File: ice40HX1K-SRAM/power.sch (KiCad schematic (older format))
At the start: 7 parts

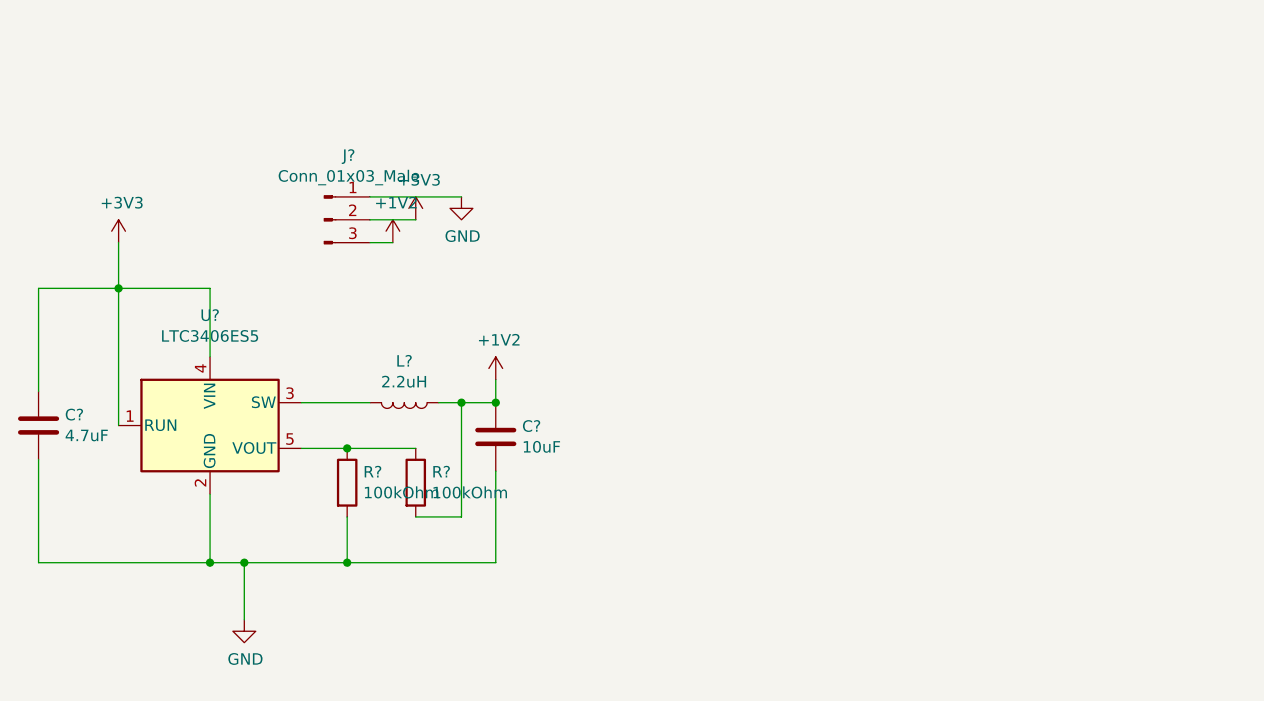
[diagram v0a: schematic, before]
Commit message: Started USB => ice40 HX1K Bridge with ATSAMD11C14A
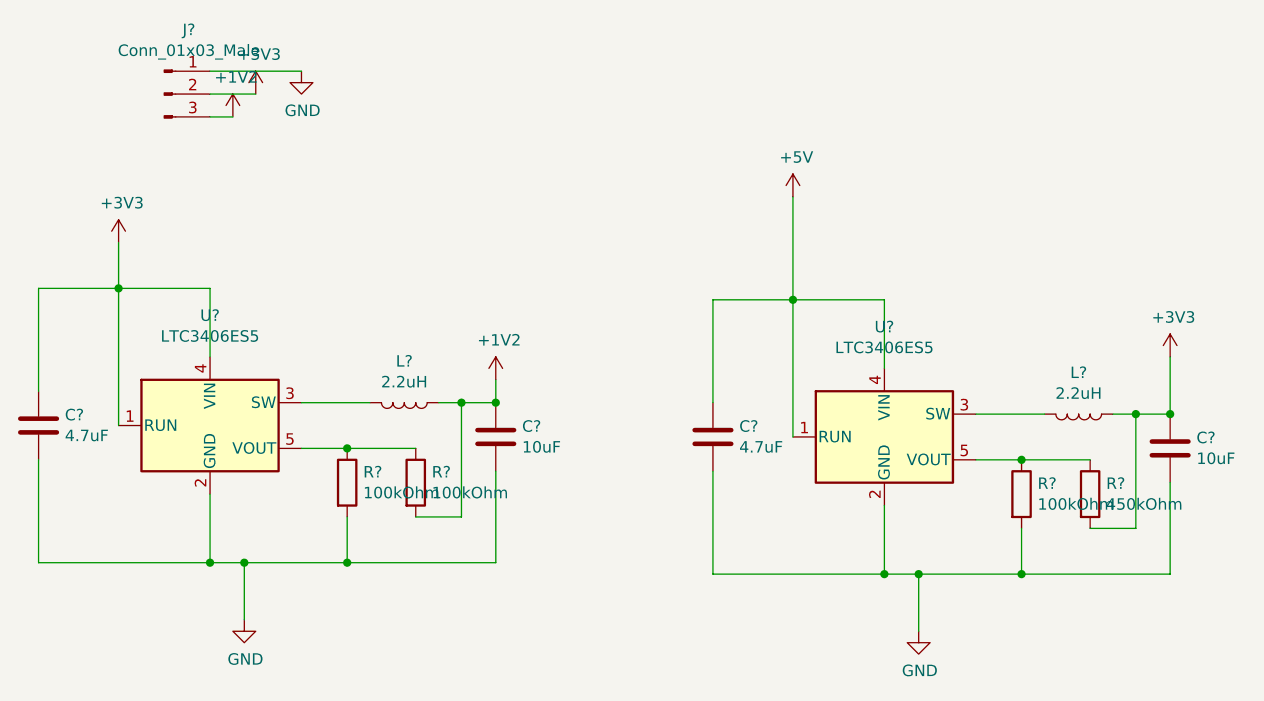
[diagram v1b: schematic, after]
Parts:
- added C?: 10uF, Capacitor_SMD:C_1206_3216Metric, symbol Device:C
- added C?: 4.7uF, Capacitor_SMD:C_1206_3216Metric, symbol Device:C
- added L?: 2.2uH, Inductor_SMD:L_1210_3225Metric, symbol Device:L
- added R?: 100kOhm, Resistor_SMD:R_1206_3216Metric, symbol Device:R
- added R?: 450kOhm, Resistor_SMD:R_0402_1005Metric, symbol Device:R
- added U?: LTC3406ES5, Package_TO_SOT_SMD:TSOT-23-5, symbol Regulator_Switching:LTC3406ES5
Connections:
- net +3V3: now also C?.1, L?.1, R?.2
- net GND: now also C?.2, C?.2, R?.2, U?.2 (GND)
- new net: L?.2, U?.3 (SW)
- new net: R?.1, R?.1, U?.5 (VOUT)
- new net +5V: C?.1, U?.1 (RUN), U?.4 (VIN)
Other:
- moved on the sheet: J?
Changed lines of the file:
@@
 $Descr A4 11693 8268
 encoding utf-8
-Sheet 2 6
+Sheet 2 8
 Title ""
 Date ""
@@
 L Connector:Conn_01x03_Male J?
 U 1 1 5E5E2652
-P 2350 1600
-F 0 "J?" H 2458 1881 50  0000 C CNN
-F 1 "Conn_01x03_Male" H 2458 1790 50  0000 C CNN
-F 2 "Connector_PinHeader_2.54mm:PinHeader_1x03_P2.54mm_Vertical" H 2350 1600 50  0001 C CNN
-F 3 "~" H 2350 1600 50  0001 C CNN
-	1    2350 1600
+P 1650 1050
+F 0 "J?" H 1758 1331 50  0000 C CNN
+F 1 "Conn_01x03_Male" H 1758 1240 50  0000 C CNN
+F 2 "Connector_PinHeader_2.54mm:PinHeader_1x03_P2.54mm_Vertical" H 1650 1050 50  0001 C CNN
+F 3 "~" H 1650 1050 50  0001 C CNN
+	1    1650 1050
 	1    0    0    -1
 $EndComp
@@
 L power:GND #PWR?
 U 1 1 5E5E2658
-P 2950 1500
-F 0 "#PWR?" H 2950 1250 50  0001 C CNN
-F 1 "GND" H 2955 1327 50  0000 C CNN
-F 2 "" H 2950 1500 50  0001 C CNN
-F 3 "" H 2950 1500 50  0001 C CNN
-	1    2950 1500
+P 2250 950
+F 0 "#PWR?" H 2250 700 50  0001 C CNN
+F 1 "GND" H 2255 777 50  0000 C CNN
+F 2 "" H 2250 950 50  0001 C CNN
+F 3 "" H 2250 950 50  0001 C CNN
+	1    2250 950
 	1    0    0    -1
 $EndComp
@@
 L power:+3V3 #PWR?
 U 1 1 5E5E265E
-P 2750 1600
-F 0 "#PWR?" H 2750 1450 50  0001 C CNN
-F 1 "+3V3" H 2765 1773 50  0000 C CNN
-F 2 "" H 2750 1600 50  0001 C CNN
-F 3 "" H 2750 1600 50  0001 C CNN
-	1    2750 1600
+P 2050 1050
+F 0 "#PWR?" H 2050 900 50  0001 C CNN
+F 1 "+3V3" H 2065 1223 50  0000 C CNN
+F 2 "" H 2050 1050 50  0001 C CNN
+F 3 "" H 2050 1050 50  0001 C CNN
+	1    2050 1050
 	1    0    0    -1
 $EndComp
@@
 L power:+1V2 #PWR?
 U 1 1 5E5E2664
-P 2650 1700
-F 0 "#PWR?" H 2650 1550 50  0001 C CNN
-F 1 "+1V2" H 2665 1873 50  0000 C CNN
-F 2 "" H 2650 1700 50  0001 C CNN
-F 3 "" H 2650 1700 50  0001 C CNN
-	1    2650 1700
-	1    0    0    -1
-$EndComp
-Wire Wire Line
-	2550 1700 2650 1700
-Wire Wire Line
-	2550 1600 2750 1600
-Wire Wire Line
-	2550 1500 2950 1500
+P 1950 1150
+F 0 "#PWR?" H 1950 1000 50  0001 C CNN
+F 1 "+1V2" H 1965 1323 50  0000 C CNN
+F 2 "" H 1950 1150 50  0001 C CNN
+F 3 "" H 1950 1150 50  0001 C CNN
+	1    1950 1150
+	1    0    0    -1
+$EndComp
+Wire Wire Line
+	1850 1150 1950 1150
+Wire Wire Line
+	1850 1050 2050 1050
+Wire Wire Line
+	1850 950  2250 950
+$Comp
+L Regulator_Switching:LTC3406ES5 U?
+U 1 1 5E5F3EED
+P 4800 2550
+F 0 "U?" H 4800 3031 50  0000 C CNN
+F 1 "LTC3406ES5" H 4800 2940 50  0000 C CNN
+F 2 "Package_TO_SOT_SMD:TSOT-23-5" H 5500 2300 50  0001 C CNN
+F 3 "https://www.analog.com/media/en/technical-documentation/data-sheets/3406b12fs.pdf" H 4800 2500 50  0001 C CNN
+	1    4800 2550
+	1    0    0    -1
+$EndComp
+$Comp
+L Device:L L?
+U 1 1 5E5F3EF3
+P 5650 2450
+F 0 "L?" V 5469 2450 50  0000 C CNN
+F 1 "2.2uH" V 5560 2450 50  0000 C CNN
+F 2 "Inductor_SMD:L_1210_3225Metric" H 5650 2450 50  0001 C CNN
+F 3 "~" H 5650 2450 50  0001 C CNN
+	1    5650 2450
+	0    1    1    0
+$EndComp
+$Comp
+L Device:C C?
+U 1 1 5E5F3EF9
+P 6050 2600
+F 0 "C?" H 6165 2646 50  0000 L CNN
+F 1 "10uF" H 6165 2555 50  0000 L CNN
+F 2 "Capacitor_SMD:C_1206_3216Metric" H 6088 2450 50  0001 C CNN
+F 3 "~" H 6050 2600 50  0001 C CNN
+	1    6050 2600
+	1    0    0    -1
+$EndComp
+$Comp
+L Device:C C?
+U 1 1 5E5F3EFF
+P 4050 2550
+F 0 "C?" H 4165 2596 50  0000 L CNN
+F 1 "4.7uF" H 4165 2505 50  0000 L CNN
+F 2 "Capacitor_SMD:C_1206_3216Metric" H 4088 2400 50  0001 C CNN
+F 3 "~" H 4050 2550 50  0001 C CNN
+	1    4050 2550
+	1    0    0    -1
+$EndComp
+$Comp
+L Device:R R?
+U 1 1 5E5F3F05
+P 5400 2800
+F 0 "R?" H 5470 2846 50  0000 L CNN
+F 1 "100kOhm" H 5470 2755 50  0000 L CNN
+F 2 "Resistor_SMD:R_1206_3216Metric" V 5330 2800 50  0001 C CNN
+F 3 "~" H 5400 2800 50  0001 C CNN
+	1    5400 2800
+	1    0    0    -1
+$EndComp
+$Comp
+L Device:R R?
+U 1 1 5E5F3F0B
+P 5700 2800
+F 0 "R?" H 5770 2846 50  0000 L CNN
+F 1 "450kOhm" H 5770 2755 50  0000 L CNN
+F 2 "Resistor_SMD:R_0402_1005Metric" V 5630 2800 50  0001 C CNN
+F 3 "~" H 5700 2800 50  0001 C CNN
+	1    5700 2800
+	1    0    0    -1
+$EndComp
+Wire Wire Line
+	5200 2450 5500 2450
+Wire Wire Line
+	5800 2450 5900 2450
+Wire Wire Line
+	5200 2650 5400 2650
+Wire Wire Line
+	5400 2650 5700 2650
+Connection ~ 5400 2650
+Wire Wire Line
+	5700 2950 5900 2950
+Wire Wire Line
+	5900 2950 5900 2450
+Connection ~ 5900 2450
+Wire Wire Line
+	5900 2450 6050 2450
+Wire Wire Line
+	4800 2250 4800 1950
+Wire Wire Line
+	4800 1950 4400 1950
+Wire Wire Line
+	4400 1950 4400 2550
+Wire Wire Line
+	4050 2400 4050 1950
+Wire Wire Line
+	4050 1950 4400 1950
+Connection ~ 4400 1950
+Wire Wire Line
+	4050 2700 4050 3150
+Wire Wire Line
+	4050 3150 4800 3150
+Wire Wire Line
+	5400 3150 5400 2950
+Wire Wire Line
+	4800 2850 4800 3150
+Connection ~ 4800 3150
+Wire Wire Line
+	4800 3150 4950 3150
+Wire Wire Line
+	5400 3150 6050 3150
+Wire Wire Line
+	6050 3150 6050 2750
+Connection ~ 5400 3150
+Connection ~ 6050 2450
+$Comp
+L power:GND #PWR?
+U 1 1 5E5F3F31
+P 4950 3400
+F 0 "#PWR?" H 4950 3150 50  0001 C CNN
+F 1 "GND" H 4955 3227 50  0000 C CNN
+F 2 "" H 4950 3400 50  0001 C CNN
+F 3 "" H 4950 3400 50  0001 C CNN
+	1    4950 3400
+	1    0    0    -1
+$EndComp
+Wire Wire Line
+	4950 3150 4950 3400
+Connection ~ 4950 3150
+Wire Wire Line
+	4950 3150 5400 3150
+$Comp
+L power:+3V3 #PWR?
+U 1 1 5E5F5466
+P 6050 2200
+F 0 "#PWR?" H 6050 2050 50  0001 C CNN
+F 1 "+3V3" H 6065 2373 50  0000 C CNN
+F 2 "" H 6050 2200 50  0001 C CNN
+F 3 "" H 6050 2200 50  0001 C CNN
+	1    6050 2200
+	1    0    0    -1
+$EndComp
+Wire Wire Line
+	6050 2200 6050 2450
+$Comp
+L power:+5V #PWR?
+U 1 1 5E5F763C
+P 4400 1500
+F 0 "#PWR?" H 4400 1350 50  0001 C CNN
+F 1 "+5V" H 4415 1673 50  0000 C CNN
+F 2 "" H 4400 1500 50  0001 C CNN
+F 3 "" H 4400 1500 50  0001 C CNN
+	1    4400 1500
+	1    0    0    -1
+$EndComp
+Wire Wire Line
+	4400 1500 4400 1950
 $EndSCHEMATC
